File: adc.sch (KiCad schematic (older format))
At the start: 50 parts, among them J1 Conn_01x08_Male, J2 Conn_01x06_Male, J3 Conn_01x08_Male, J4 Conn_01x10_Male, J5 Conn_02x08_Odd_Even, J6 Conn_02x08_Odd_Even, J7 Conn_02x08_Odd_Even, U1 ADC128D818, U2 ADC128D818, U3 ADC128D818

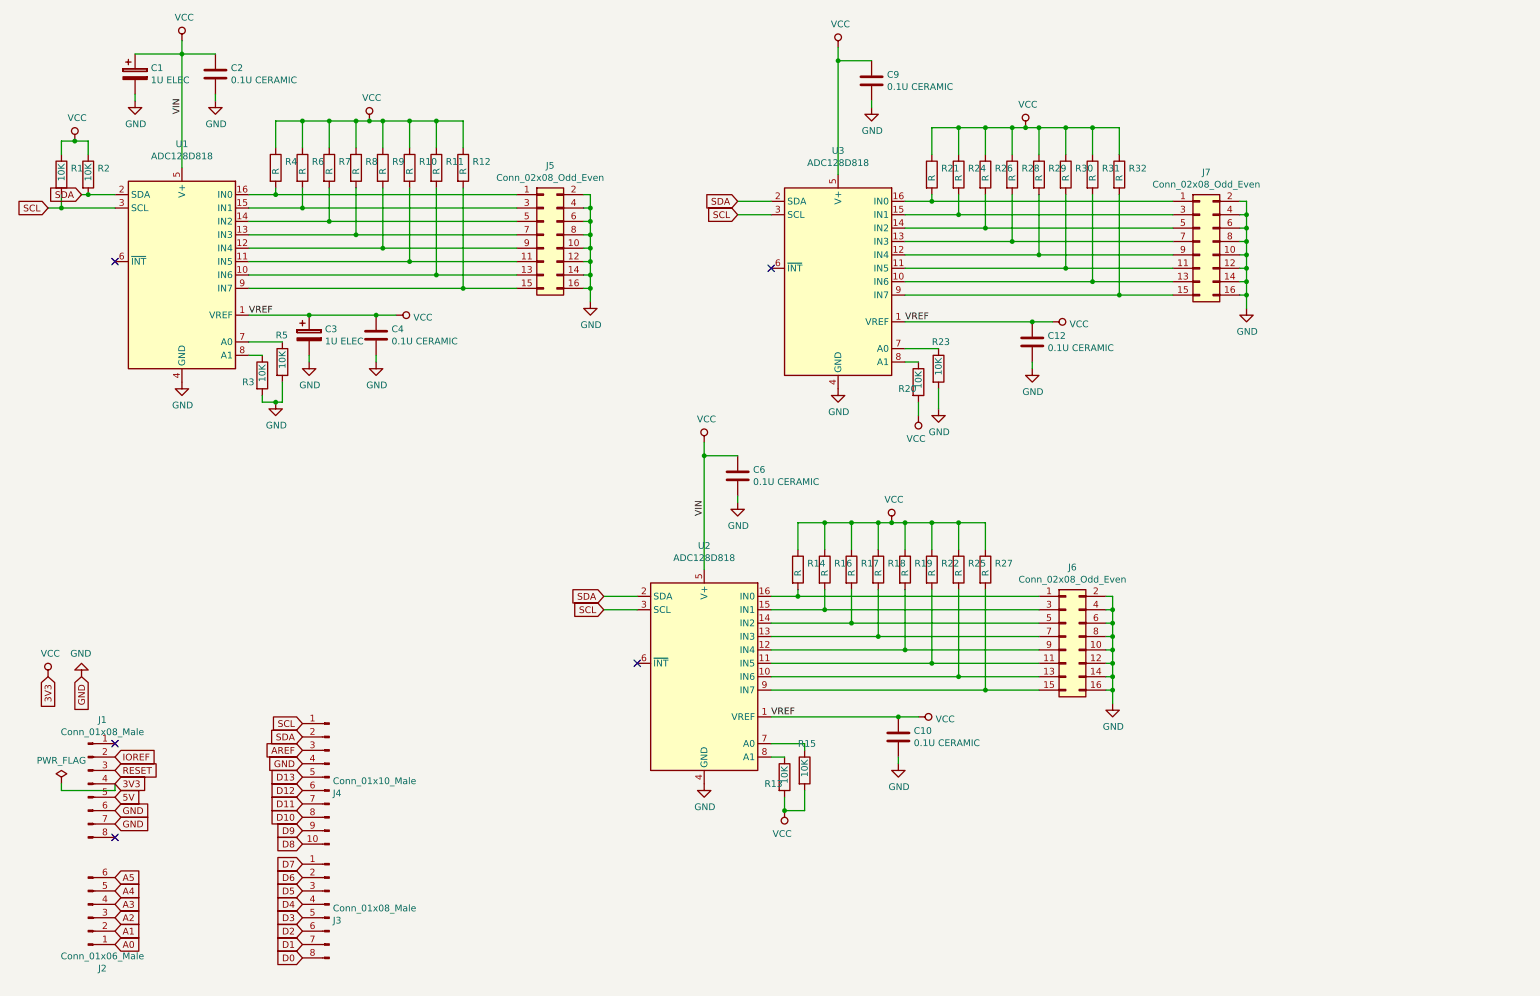
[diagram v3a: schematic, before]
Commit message: change electrolytics to caps, ceramics 1206 -> 1210
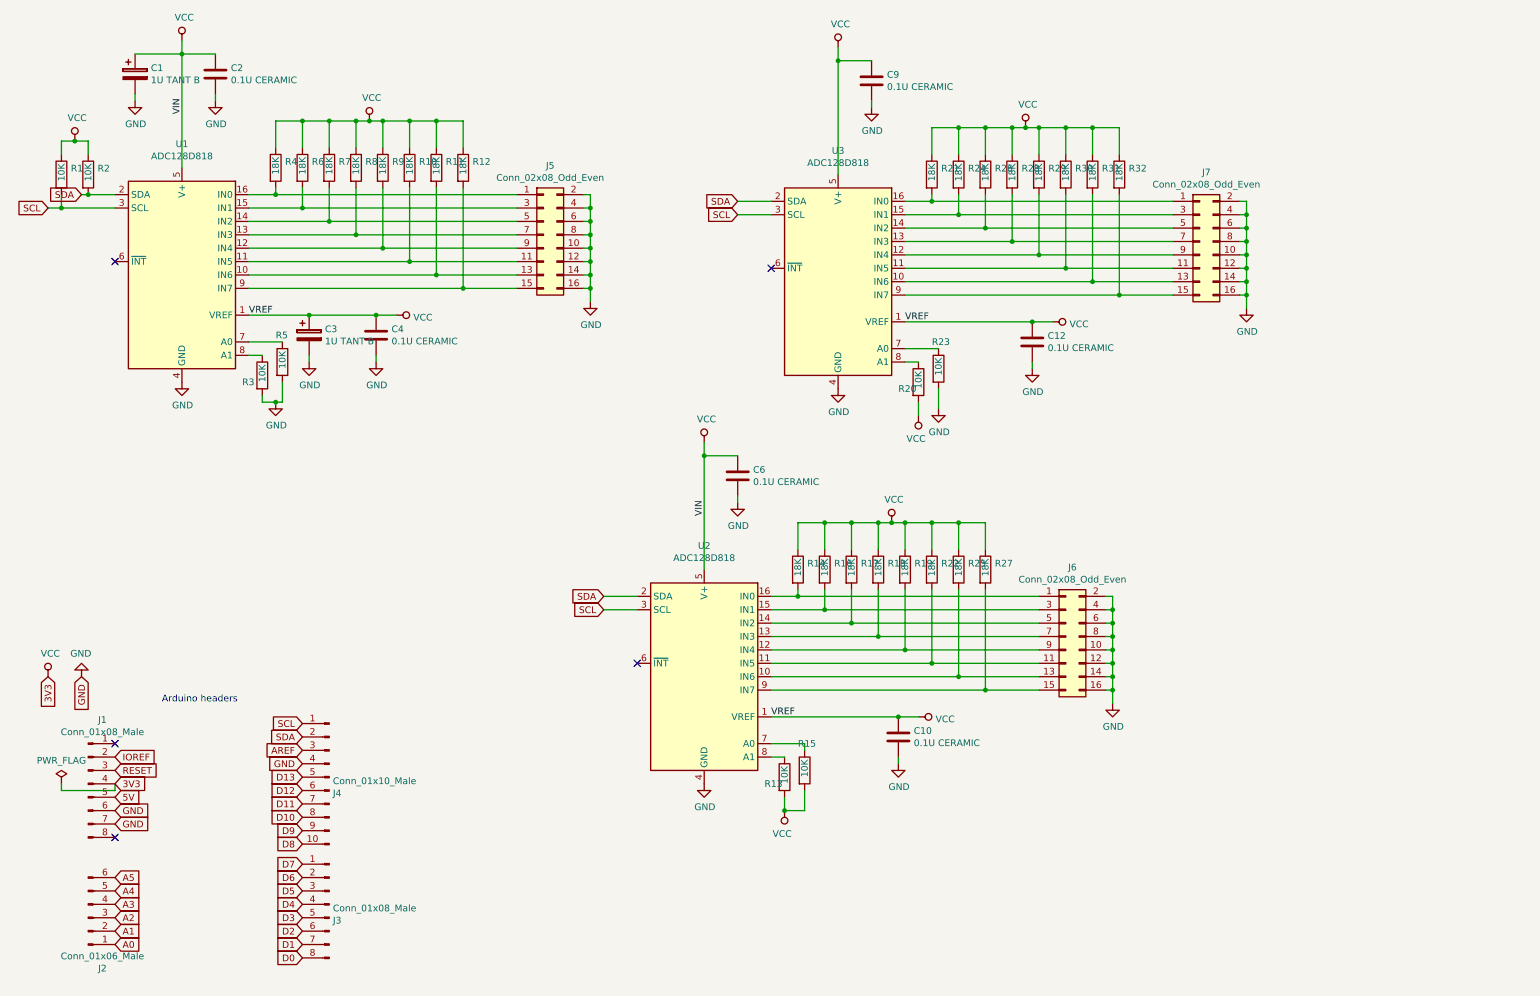
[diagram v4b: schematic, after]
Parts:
- C1, C3: value 1U ELEC -> 1U TANT B; footprint Capacitors_SMD:CP_Elec_5x5.8 -> Capacitors_Tantalum_SMD:CP_Tantalum_Case-B_EIA-3528-21_Hand
- C10, C12, C2, C4, C6, C9: footprint Capacitors_SMD:C_1206_HandSoldering -> Capacitors_SMD:C_1210_HandSoldering
- R10, R11, R12, R14, R16, R17, R18, R19, R21, R24, R25, R26, R27, R28, R29, R30, R31, R32, R4, R6, R7, R8, R9: value R -> 18K
- R22: value R -> 18k
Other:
- note added: "Arduino headers"
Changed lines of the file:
@@
 P 2450 1600
 F 0 "R4" H 2520 1646 50  0000 L CNN
-F 1 "R" V 2450 1550 50  0000 L CNN
+F 1 "18K" V 2450 1550 50  0000 L CNN
 F 2 "Resistors_SMD:R_1206_HandSoldering" V 2380 1600 50  0001 C CNN
 F 3 "~" H 2450 1600 50  0001 C CNN
@@
 P 2650 1600
 F 0 "R6" H 2720 1646 50  0000 L CNN
-F 1 "R" V 2650 1550 50  0000 L CNN
+F 1 "18K" V 2650 1550 50  0000 L CNN
 F 2 "Resistors_SMD:R_1206_HandSoldering" V 2580 1600 50  0001 C CNN
 F 3 "~" H 2650 1600 50  0001 C CNN
@@
 P 2850 1600
 F 0 "R7" H 2920 1646 50  0000 L CNN
-F 1 "R" V 2850 1550 50  0000 L CNN
+F 1 "18K" V 2850 1550 50  0000 L CNN
 F 2 "Resistors_SMD:R_1206_HandSoldering" V 2780 1600 50  0001 C CNN
 F 3 "~" H 2850 1600 50  0001 C CNN
@@
 P 3050 1600
 F 0 "R8" H 3120 1646 50  0000 L CNN
-F 1 "R" V 3050 1550 50  0000 L CNN
+F 1 "18K" V 3050 1550 50  0000 L CNN
 F 2 "Resistors_SMD:R_1206_HandSoldering" V 2980 1600 50  0001 C CNN
 F 3 "~" H 3050 1600 50  0001 C CNN
@@
 P 3250 1600
 F 0 "R9" H 3320 1646 50  0000 L CNN
-F 1 "R" V 3250 1550 50  0000 L CNN
+F 1 "18K" V 3250 1550 50  0000 L CNN
 F 2 "Resistors_SMD:R_1206_HandSoldering" V 3180 1600 50  0001 C CNN
 F 3 "~" H 3250 1600 50  0001 C CNN
@@
 P 3450 1600
 F 0 "R10" H 3520 1646 50  0000 L CNN
-F 1 "R" V 3450 1550 50  0000 L CNN
+F 1 "18K" V 3450 1550 50  0000 L CNN
 F 2 "Resistors_SMD:R_1206_HandSoldering" V 3380 1600 50  0001 C CNN
 F 3 "~" H 3450 1600 50  0001 C CNN
@@
 P 3650 1600
 F 0 "R11" H 3720 1646 50  0000 L CNN
-F 1 "R" V 3650 1550 50  0000 L CNN
+F 1 "18K" V 3650 1550 50  0000 L CNN
 F 2 "Resistors_SMD:R_1206_HandSoldering" V 3580 1600 50  0001 C CNN
 F 3 "~" H 3650 1600 50  0001 C CNN
@@
 P 3850 1600
 F 0 "R12" H 3920 1646 50  0000 L CNN
-F 1 "R" V 3850 1550 50  0000 L CNN
+F 1 "18K" V 3850 1550 50  0000 L CNN
 F 2 "Resistors_SMD:R_1206_HandSoldering" V 3780 1600 50  0001 C CNN
 F 3 "~" H 3850 1600 50  0001 C CNN
@@
 F 0 "C4" H 3315 2896 50  0000 L CNN
 F 1 "0.1U CERAMIC" H 3315 2805 50  0000 L CNN
-F 2 "Capacitors_SMD:C_1206_HandSoldering" H 3238 2700 50  0001 C CNN
+F 2 "Capacitors_SMD:C_1210_HandSoldering" H 3238 2700 50  0001 C CNN
 F 3 "~" H 3200 2850 50  0001 C CNN
 	1    3200 2850
@@
 P 2700 2850
 F 0 "C3" H 2818 2896 50  0000 L CNN
-F 1 "1U ELEC" H 2818 2805 50  0000 L CNN
-F 2 "Capacitors_SMD:CP_Elec_5x5.8" H 2738 2700 50  0001 C CNN
+F 1 "1U TANT B" H 2818 2805 50  0000 L CNN
+F 2 "Capacitors_Tantalum_SMD:CP_Tantalum_Case-B_EIA-3528-21_Hand" H 2738 2700 50  0001 C CNN
 F 3 "~" H 2700 2850 50  0001 C CNN
 	1    2700 2850
@@
 F 0 "C2" H 2115 946 50  0000 L CNN
 F 1 "0.1U CERAMIC" H 2115 855 50  0000 L CNN
-F 2 "Capacitors_SMD:C_1206_HandSoldering" H 2038 750 50  0001 C CNN
+F 2 "Capacitors_SMD:C_1210_HandSoldering" H 2038 750 50  0001 C CNN
 F 3 "~" H 2000 900 50  0001 C CNN
 	1    2000 900
@@
 P 1400 900
 F 0 "C1" H 1518 946 50  0000 L CNN
-F 1 "1U ELEC" H 1518 855 50  0000 L CNN
-F 2 "Capacitors_SMD:CP_Elec_5x5.8" H 1438 750 50  0001 C CNN
+F 1 "1U TANT B" H 1518 855 50  0000 L CNN
+F 2 "Capacitors_Tantalum_SMD:CP_Tantalum_Case-B_EIA-3528-21_Hand" H 1438 750 50  0001 C CNN
 F 3 "~" H 1400 900 50  0001 C CNN
 	1    1400 900
@@
 P 7350 1650
 F 0 "R21" H 7420 1696 50  0000 L CNN
-F 1 "R" V 7350 1600 50  0000 L CNN
+F 1 "18K" V 7350 1600 50  0000 L CNN
 F 2 "Resistors_SMD:R_1206_HandSoldering" V 7280 1650 50  0001 C CNN
 F 3 "~" H 7350 1650 50  0001 C CNN
@@
 P 7550 1650
 F 0 "R24" H 7620 1696 50  0000 L CNN
-F 1 "R" V 7550 1600 50  0000 L CNN
+F 1 "18K" V 7550 1600 50  0000 L CNN
 F 2 "Resistors_SMD:R_1206_HandSoldering" V 7480 1650 50  0001 C CNN
 F 3 "~" H 7550 1650 50  0001 C CNN
@@
 P 7750 1650
 F 0 "R26" H 7820 1696 50  0000 L CNN
-F 1 "R" V 7750 1600 50  0000 L CNN
+F 1 "18K" V 7750 1600 50  0000 L CNN
 F 2 "Resistors_SMD:R_1206_HandSoldering" V 7680 1650 50  0001 C CNN
 F 3 "~" H 7750 1650 50  0001 C CNN
@@
 P 7950 1650
 F 0 "R28" H 8020 1696 50  0000 L CNN
-F 1 "R" V 7950 1600 50  0000 L CNN
+F 1 "18K" V 7950 1600 50  0000 L CNN
 F 2 "Resistors_SMD:R_1206_HandSoldering" V 7880 1650 50  0001 C CNN
 F 3 "~" H 7950 1650 50  0001 C CNN
@@
 P 8150 1650
 F 0 "R29" H 8220 1696 50  0000 L CNN
-F 1 "R" V 8150 1600 50  0000 L CNN
+F 1 "18K" V 8150 1600 50  0000 L CNN
 F 2 "Resistors_SMD:R_1206_HandSoldering" V 8080 1650 50  0001 C CNN
 F 3 "~" H 8150 1650 50  0001 C CNN
@@
 P 8350 1650
 F 0 "R30" H 8420 1696 50  0000 L CNN
-F 1 "R" V 8350 1600 50  0000 L CNN
+F 1 "18K" V 8350 1600 50  0000 L CNN
 F 2 "Resistors_SMD:R_1206_HandSoldering" V 8280 1650 50  0001 C CNN
 F 3 "~" H 8350 1650 50  0001 C CNN
@@
 P 8550 1650
 F 0 "R31" H 8620 1696 50  0000 L CNN
-F 1 "R" V 8550 1600 50  0000 L CNN
+F 1 "18K" V 8550 1600 50  0000 L CNN
 F 2 "Resistors_SMD:R_1206_HandSoldering" V 8480 1650 50  0001 C CNN
 F 3 "~" H 8550 1650 50  0001 C CNN
@@
 P 8750 1650
 F 0 "R32" H 8820 1696 50  0000 L CNN
-F 1 "R" V 8750 1600 50  0000 L CNN
+F 1 "18K" V 8750 1600 50  0000 L CNN
 F 2 "Resistors_SMD:R_1206_HandSoldering" V 8680 1650 50  0001 C CNN
 F 3 "~" H 8750 1650 50  0001 C CNN
@@
 F 0 "C12" H 8215 2946 50  0000 L CNN
 F 1 "0.1U CERAMIC" H 8215 2855 50  0000 L CNN
-F 2 "Capacitors_SMD:C_1206_HandSoldering" H 8138 2750 50  0001 C CNN
+F 2 "Capacitors_SMD:C_1210_HandSoldering" H 8138 2750 50  0001 C CNN
 F 3 "~" H 8100 2900 50  0001 C CNN
 	1    8100 2900
@@
 F 0 "C9" H 7015 996 50  0000 L CNN
 F 1 "0.1U CERAMIC" H 7015 905 50  0000 L CNN
-F 2 "Capacitors_SMD:C_1206_HandSoldering" H 6938 800 50  0001 C CNN
+F 2 "Capacitors_SMD:C_1210_HandSoldering" H 6938 800 50  0001 C CNN
 F 3 "~" H 6900 950 50  0001 C CNN
 	1    6900 950
@@
 P 6350 4600
 F 0 "R14" H 6420 4646 50  0000 L CNN
-F 1 "R" V 6350 4550 50  0000 L CNN
+F 1 "18K" V 6350 4550 50  0000 L CNN
 F 2 "Resistors_SMD:R_1206_HandSoldering" V 6280 4600 50  0001 C CNN
 F 3 "~" H 6350 4600 50  0001 C CNN
@@
 P 6550 4600
 F 0 "R16" H 6620 4646 50  0000 L CNN
-F 1 "R" V 6550 4550 50  0000 L CNN
+F 1 "18K" V 6550 4550 50  0000 L CNN
 F 2 "Resistors_SMD:R_1206_HandSoldering" V 6480 4600 50  0001 C CNN
 F 3 "~" H 6550 4600 50  0001 C CNN
@@
 P 6750 4600
 F 0 "R17" H 6820 4646 50  0000 L CNN
-F 1 "R" V 6750 4550 50  0000 L CNN
+F 1 "18K" V 6750 4550 50  0000 L CNN
 F 2 "Resistors_SMD:R_1206_HandSoldering" V 6680 4600 50  0001 C CNN
 F 3 "~" H 6750 4600 50  0001 C CNN
@@
 P 6950 4600
 F 0 "R18" H 7020 4646 50  0000 L CNN
-F 1 "R" V 6950 4550 50  0000 L CNN
+F 1 "18K" V 6950 4550 50  0000 L CNN
 F 2 "Resistors_SMD:R_1206_HandSoldering" V 6880 4600 50  0001 C CNN
 F 3 "~" H 6950 4600 50  0001 C CNN
@@
 P 7150 4600
 F 0 "R19" H 7220 4646 50  0000 L CNN
-F 1 "R" V 7150 4550 50  0000 L CNN
+F 1 "18K" V 7150 4550 50  0000 L CNN
 F 2 "Resistors_SMD:R_1206_HandSoldering" V 7080 4600 50  0001 C CNN
 F 3 "~" H 7150 4600 50  0001 C CNN
@@
 P 7350 4600
 F 0 "R22" H 7420 4646 50  0000 L CNN
-F 1 "R" V 7350 4550 50  0000 L CNN
+F 1 "18k" V 7350 4550 50  0000 L CNN
 F 2 "Resistors_SMD:R_1206_HandSoldering" V 7280 4600 50  0001 C CNN
 F 3 "~" H 7350 4600 50  0001 C CNN
@@
 P 7550 4600
 F 0 "R25" H 7620 4646 50  0000 L CNN
-F 1 "R" V 7550 4550 50  0000 L CNN
+F 1 "18K" V 7550 4550 50  0000 L CNN
 F 2 "Resistors_SMD:R_1206_HandSoldering" V 7480 4600 50  0001 C CNN
 F 3 "~" H 7550 4600 50  0001 C CNN
@@
 P 7750 4600
 F 0 "R27" H 7820 4646 50  0000 L CNN
-F 1 "R" V 7750 4550 50  0000 L CNN
+F 1 "18K" V 7750 4550 50  0000 L CNN
 F 2 "Resistors_SMD:R_1206_HandSoldering" V 7680 4600 50  0001 C CNN
 F 3 "~" H 7750 4600 50  0001 C CNN
@@
 F 0 "C10" H 7215 5896 50  0000 L CNN
 F 1 "0.1U CERAMIC" H 7215 5805 50  0000 L CNN
-F 2 "Capacitors_SMD:C_1206_HandSoldering" H 7138 5700 50  0001 C CNN
+F 2 "Capacitors_SMD:C_1210_HandSoldering" H 7138 5700 50  0001 C CNN
 F 3 "~" H 7100 5850 50  0001 C CNN
 	1    7100 5850
@@
 F 0 "C6" H 6015 3946 50  0000 L CNN
 F 1 "0.1U CERAMIC" H 6015 3855 50  0000 L CNN
-F 2 "Capacitors_SMD:C_1206_HandSoldering" H 5938 3750 50  0001 C CNN
+F 2 "Capacitors_SMD:C_1210_HandSoldering" H 5938 3750 50  0001 C CNN
 F 3 "~" H 5900 3900 50  0001 C CNN
 	1    5900 3900
@@
 Wire Wire Line
 	6150 5700 7100 5700
+Text Notes 1600 5600 0    50   ~ 0
+Arduino headers
 $EndSCHEMATC

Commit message: misc
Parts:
- U1, U2, U3: footprint footprints:TSSOP-16_4.4x5mm_P0.65mm -> Housings_SSOP:TSSOP-16_4.4x5mm_Pitch0.65mm
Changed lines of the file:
@@
 F 0 "U1" H 1750 3378 50  0000 C CNN
 F 1 "ADC128D818" H 1750 3287 50  0000 C CNN
-F 2 "footprints:TSSOP-16_4.4x5mm_P0.65mm" H 1750 2400 50  0001 C CIN
+F 2 "Housings_SSOP:TSSOP-16_4.4x5mm_Pitch0.65mm" H 1750 2400 50  0001 C CIN
 F 3 "http://www.ti.com/lit/ds/symlink/adc128d818.pdf" H 1750 2400 50  0001 C CNN
 	1    1750 2400
@@
 F 0 "U3" H 6650 3428 50  0000 C CNN
 F 1 "ADC128D818" H 6650 3337 50  0000 C CNN
-F 2 "footprints:TSSOP-16_4.4x5mm_P0.65mm" H 6650 2450 50  0001 C CIN
+F 2 "Housings_SSOP:TSSOP-16_4.4x5mm_Pitch0.65mm" H 6650 2450 50  0001 C CIN
 F 3 "http://www.ti.com/lit/ds/symlink/adc128d818.pdf" H 6650 2450 50  0001 C CNN
 	1    6650 2450
@@
 F 0 "U2" H 5650 6378 50  0000 C CNN
 F 1 "ADC128D818" H 5650 6287 50  0000 C CNN
-F 2 "footprints:TSSOP-16_4.4x5mm_P0.65mm" H 5650 5400 50  0001 C CIN
+F 2 "Housings_SSOP:TSSOP-16_4.4x5mm_Pitch0.65mm" H 5650 5400 50  0001 C CIN
 F 3 "http://www.ti.com/lit/ds/symlink/adc128d818.pdf" H 5650 5400 50  0001 C CNN
 	1    5650 5400

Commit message: updates + printout pdf
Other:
- note added: "1"
- note added: "2018 Nov 29"
- note added: "ADC128 Thermistor Arduino Sheild"
- note added: "Property General Atomics / Team OTheRS"
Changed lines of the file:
@@
 Text Notes 1600 5600 0    50   ~ 0
 Arduino headers
+Text Notes 7400 7500 0    79   ~ 16
+ADC128 Thermistor Arduino Sheild
+Text Notes 8150 7650 0    50   ~ 0
+2018 Nov 29
+Text Notes 10600 7650 0    50   ~ 0
+1
+Text Notes 7000 6850 0    128  ~ 0
+Property General Atomics / Team OTheRS
 $EndSCHEMATC

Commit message: idk
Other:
- note added: "Property of Team OTheRS\nJacob Killelea"
- note removed: "Property General Atomics / Team OTheRS"
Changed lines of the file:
@@
 Text Notes 10600 7650 0    50   ~ 0
 1
-Text Notes 7000 6850 0    128  ~ 0
-Property General Atomics / Team OTheRS
+Text Notes 7000 7000 0    128  ~ 0
+Property  of Team OTheRS\nJacob Killelea
 $EndSCHEMATC
